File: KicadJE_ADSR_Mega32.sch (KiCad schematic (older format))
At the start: 68 parts, among them J102 OUT2, J105 IN1, J106 IN2, J107 CV2, J108 CV1

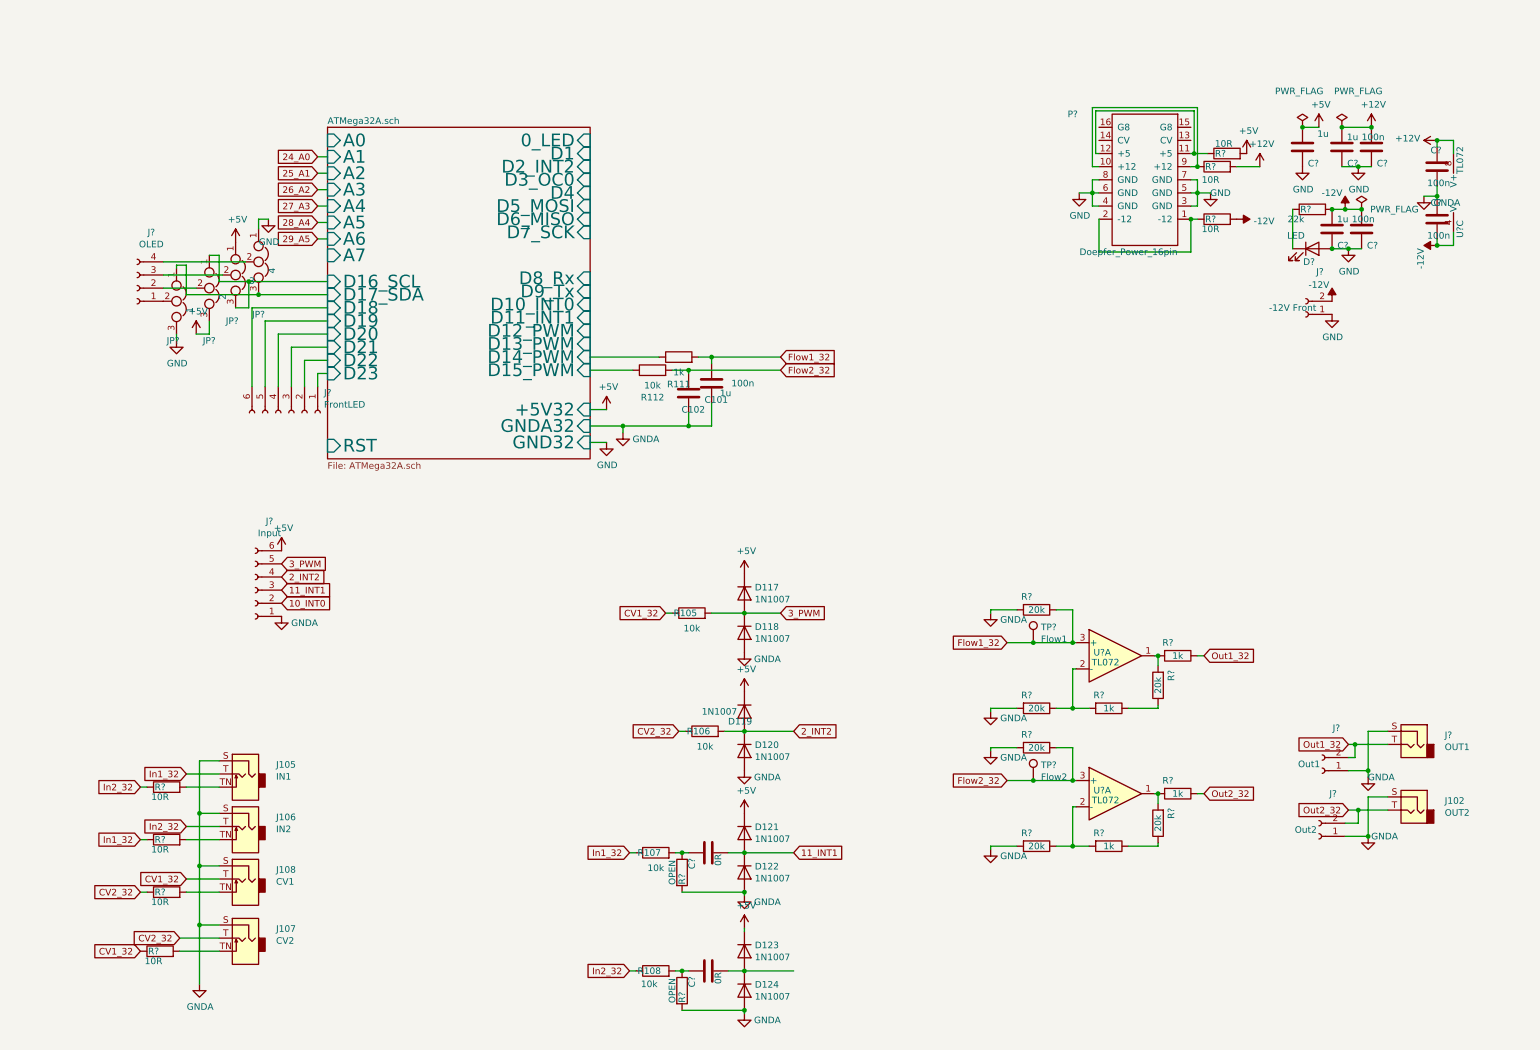
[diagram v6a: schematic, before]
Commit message: Importing Encoder from Midi2CV
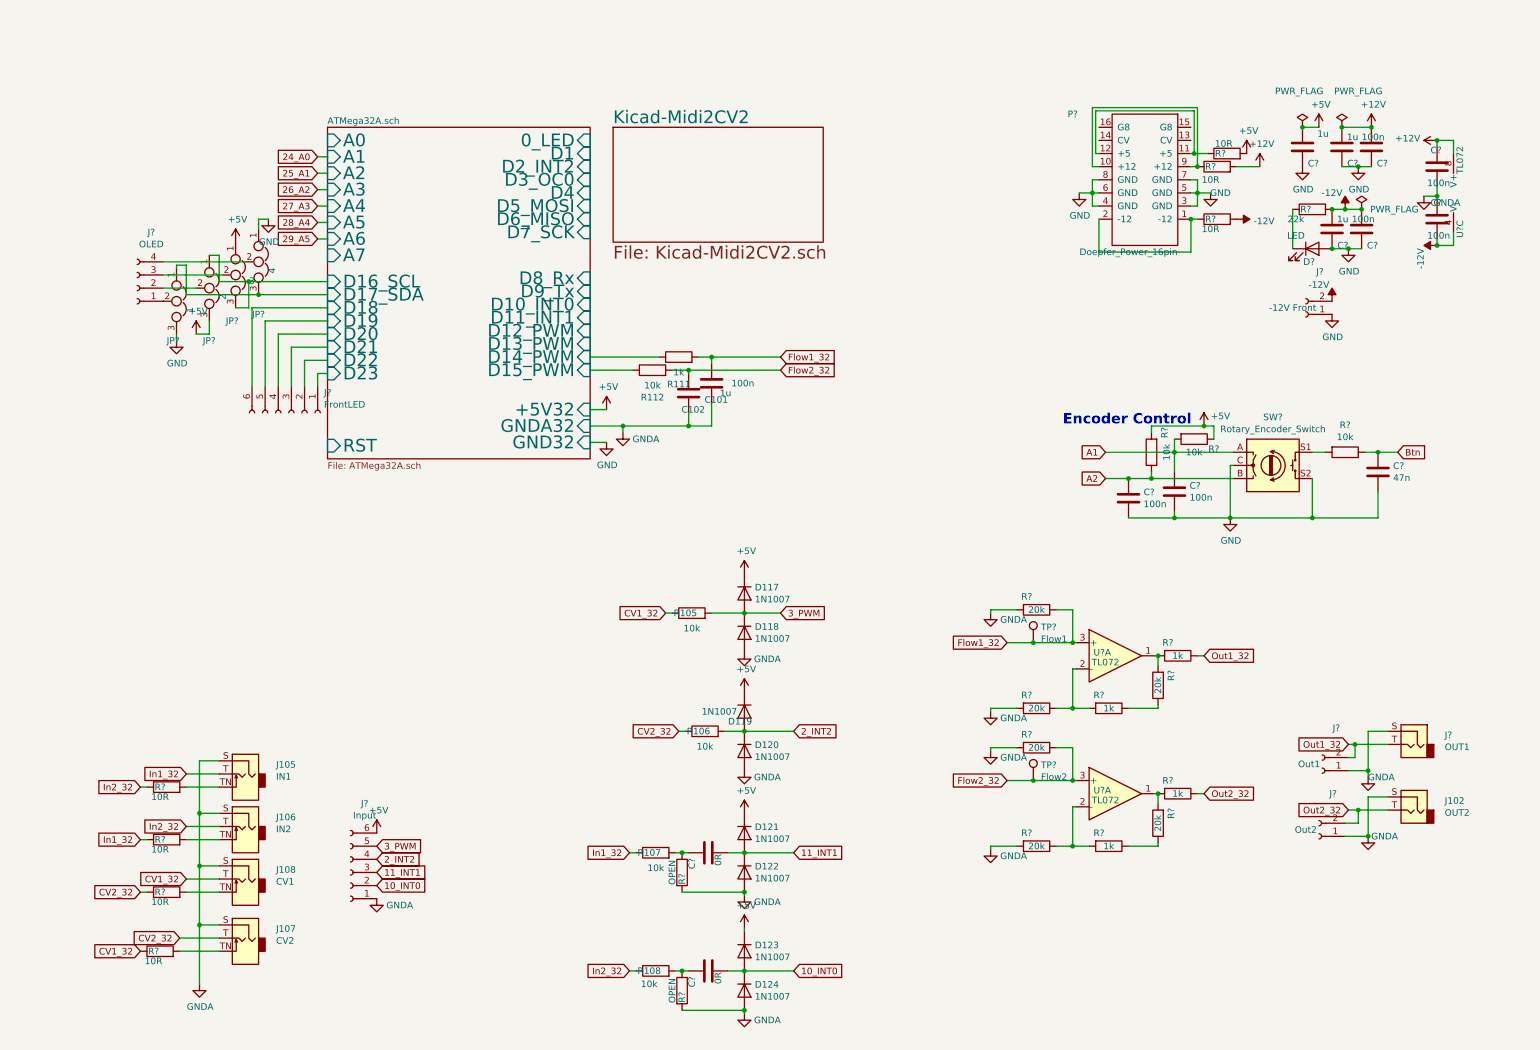
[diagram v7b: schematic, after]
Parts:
- added C? (x2): 100n, Capacitor_SMD:C_0805_2012Metric_Pad1.15x1.40mm_HandSolder, symbol Device:C
- added C?: 47n, Capacitor_SMD:C_0805_2012Metric_Pad1.15x1.40mm_HandSolder, symbol Device:C
- added R? (x3): 10k, Resistor_SMD:R_0805_2012Metric_Pad1.15x1.40mm_HandSolder, symbol Device:R
- added SW?: Rotary_Encoder_Switch, Rotary_Encoder:RotaryEncoder_Alps_EC11E-Switch_Vertical_H20mm, symbol Device:Rotary_Encoder_Switch
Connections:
- net +5V: now also R?.1, R?.2
- net 10_INT0: now also C?.2, D123.2 (A), D124.1 (K)
- net GND: now also C?.2, C?.2, C?.2, SW?.C, SW?.S2
- new net: R?.2, SW?.S1
- new net A1: C?.1, R?.2, SW?.A
- new net A2: C?.1, R?.1, SW?.B
- new net Btn: C?.1, R?.1
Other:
- note added: "Encoder Control"
- moved on the sheet: J?
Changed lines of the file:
@@
 $Descr A4 11693 8268
 encoding utf-8
-Sheet 2 3
+Sheet 2 4
 Title "Kicad_JE_ADSR_Mega32"
 Date "2019-05-13"
@@
 	1    0    0    -1
 $EndComp
-Text GLabel 2075 4500 2    50   Input ~ 0
+Text GLabel 2800 6650 2    50   Input ~ 0
 10_INT0
 Text GLabel 5975 6400 2    50   Input ~ 0
@@
 AR Path="/5F49A670/60E5BC60" Ref="U?"  Part="3"
 AR Path="/60E5BC60" Ref="U?"  Part="3"
+AR Path="/608CA457/60E5BC60" Ref="U?"  Part="3"
 F 0 "U?" V 10750 1100 50  0000 C CNN
 F 1 "TL072" V 10750 1625 50  0000 C CNN
@@
 L Connector:Conn_01x06_Female J?
 U 1 1 610AFCC8
-P 1875 4400
-F 0 "J?" H 1767 3875 50  0000 C CNN
-F 1 "Input" H 1767 3966 50  0000 C CNN
-F 2 "Connector_PinSocket_2.54mm:PinSocket_1x06_P2.54mm_Vertical" H 1875 4400 50  0001 C CNN
-F 3 "~" H 1875 4400 50  0001 C CNN
-	1    1875 4400
+P 2600 6550
+F 0 "J?" H 2492 6025 50  0000 C CNN
+F 1 "Input" H 2492 6116 50  0000 C CNN
+F 2 "Connector_PinSocket_2.54mm:PinSocket_1x06_P2.54mm_Vertical" H 2600 6550 50  0001 C CNN
+F 3 "~" H 2600 6550 50  0001 C CNN
+	1    2600 6550
 	-1   0    0    1
 $EndComp
-Text GLabel 2075 4200 2    50   Input ~ 0
+Text GLabel 2800 6350 2    50   Input ~ 0
 3_PWM
-Text GLabel 2075 4300 2    50   Input ~ 0
+Text GLabel 2800 6450 2    50   Input ~ 0
 2_INT2
-Text GLabel 2075 4400 2    50   Input ~ 0
+Text GLabel 2800 6550 2    50   Input ~ 0
 11_INT1
 $Comp
 L power:GNDA #PWR?
 U 1 1 610D759E
-P 2075 4600
+P 2800 6750
 AR Path="/610D759E" Ref="#PWR?"  Part="1"
 AR Path="/5CD3F059/610D759E" Ref="#PWR?"  Part="1"
 AR Path="/608CA457/610D759E" Ref="#PWR?"  Part="1"
-F 0 "#PWR?" H 2075 4350 50  0001 C CNN
-F 1 "GNDA" H 2250 4550 50  0000 C CNN
-F 2 "" H 2075 4600 50  0001 C CNN
-F 3 "" H 2075 4600 50  0001 C CNN
-	1    2075 4600
+F 0 "#PWR?" H 2800 6500 50  0001 C CNN
+F 1 "GNDA" H 2975 6700 50  0000 C CNN
+F 2 "" H 2800 6750 50  0001 C CNN
+F 3 "" H 2800 6750 50  0001 C CNN
+	1    2800 6750
 	1    0    0    -1
 $EndComp
@@
 L power:+5V #PWR?
 U 1 1 610D7AE4
-P 2075 4100
-F 0 "#PWR?" H 2075 3950 50  0001 C CNN
-F 1 "+5V" H 2090 4273 50  0000 C CNN
-F 2 "" H 2075 4100 50  0001 C CNN
-F 3 "" H 2075 4100 50  0001 C CNN
-	1    2075 4100
+P 2800 6250
+F 0 "#PWR?" H 2800 6100 50  0001 C CNN
+F 1 "+5V" H 2815 6423 50  0000 C CNN
+F 2 "" H 2800 6250 50  0001 C CNN
+F 3 "" H 2800 6250 50  0001 C CNN
+	1    2800 6250
 	1    0    0    -1
 $EndComp
@@
 	1    0    0    -1
 $EndComp
+$Sheet
+S 4600 875  1600 875
+U 6120CBE2
+F0 "Kicad-Midi2CV2" 97
+F1 "Kicad-Midi2CV2.sch" 97
+$EndSheet
+$Comp
+L Device:C C?
+U 1 1 6125DC4B
+P 8525 3700
+F 0 "C?" H 8640 3746 50  0000 L CNN
+F 1 "100n" H 8640 3655 50  0000 L CNN
+F 2 "Capacitor_SMD:C_0805_2012Metric_Pad1.15x1.40mm_HandSolder" H 8563 3550 50  0001 C CNN
+F 3 "~" H 8525 3700 50  0001 C CNN
+	1    8525 3700
+	1    0    0    -1
+$EndComp
+$Comp
+L Device:C C?
+U 1 1 6125DC51
+P 8875 3650
+F 0 "C?" H 8990 3696 50  0000 L CNN
+F 1 "100n" H 8990 3605 50  0000 L CNN
+F 2 "Capacitor_SMD:C_0805_2012Metric_Pad1.15x1.40mm_HandSolder" H 8913 3500 50  0001 C CNN
+F 3 "~" H 8875 3650 50  0001 C CNN
+	1    8875 3650
+	1    0    0    -1
+$EndComp
+Text GLabel 10575 3350 2    50   Input ~ 0
+Btn
+$Comp
+L power:GND #PWR?
+U 1 1 6125DC58
+P 9300 3850
+F 0 "#PWR?" H 9300 3600 50  0001 C CNN
+F 1 "GND" H 9305 3677 50  0000 C CNN
+F 2 "" H 9300 3850 50  0001 C CNN
+F 3 "" H 9300 3850 50  0001 C CNN
+	1    9300 3850
+	1    0    0    -1
+$EndComp
+$Comp
+L Device:R R?
+U 1 1 6125DC5E
+P 10175 3350
+F 0 "R?" V 9968 3350 50  0000 C CNN
+F 1 "10k" V 10059 3350 50  0000 C CNN
+F 2 "Resistor_SMD:R_0805_2012Metric_Pad1.15x1.40mm_HandSolder" V 10105 3350 50  0001 C CNN
+F 3 "~" H 10175 3350 50  0001 C CNN
+	1    10175 3350
+	0    1    1    0
+$EndComp
+$Comp
+L Device:C C?
+U 1 1 6125DC64
+P 10425 3500
+F 0 "C?" H 10540 3546 50  0000 L CNN
+F 1 "47n" H 10540 3455 50  0000 L CNN
+F 2 "Capacitor_SMD:C_0805_2012Metric_Pad1.15x1.40mm_HandSolder" H 10463 3350 50  0001 C CNN
+F 3 "~" H 10425 3500 50  0001 C CNN
+	1    10425 3500
+	1    0    0    -1
+$EndComp
+Text GLabel 8350 3350 0    50   Input ~ 0
+A1
+Text Notes 8025 3150 0    79   ~ 16
+Encoder Control
+Text GLabel 8350 3550 0    50   Input ~ 0
+A2
+Wire Wire Line
+	9925 3550 9925 3850
+$Comp
+L power:+5V #PWR?
+U 1 1 6125DC71
+P 9100 3150
+F 0 "#PWR?" H 9100 3000 50  0001 C CNN
+F 1 "+5V" H 9225 3225 50  0000 C CNN
+F 2 "" H 9100 3150 50  0001 C CNN
+F 3 "" H 9100 3150 50  0001 C CNN
+	1    9100 3150
+	1    0    0    -1
+$EndComp
+Wire Wire Line
+	9925 3350 10025 3350
+Wire Wire Line
+	10325 3350 10425 3350
+Wire Wire Line
+	10575 3350 10425 3350
+Connection ~ 10425 3350
+Wire Wire Line
+	10425 3650 10425 3850
+Wire Wire Line
+	10425 3850 9925 3850
+Connection ~ 9925 3850
+Wire Wire Line
+	8875 3800 8875 3850
+Connection ~ 8875 3850
+Wire Wire Line
+	8875 3500 8875 3350
+Connection ~ 8875 3350
+Wire Wire Line
+	8875 3350 9325 3350
+$Comp
+L Device:Rotary_Encoder_Switch SW?
+U 1 1 6125DC86
+P 9625 3450
+AR Path="/608CA457/6120CBE2/6125DC86" Ref="SW?"  Part="1"
+AR Path="/608CA457/6125DC86" Ref="SW?"  Part="1"
+F 0 "SW?" H 9625 3817 50  0000 C CNN
+F 1 "Rotary_Encoder_Switch" H 9625 3726 50  0000 C CNN
+F 2 "Rotary_Encoder:RotaryEncoder_Alps_EC11E-Switch_Vertical_H20mm" H 9475 3610 50  0001 C CNN
+F 3 "~" H 9625 3710 50  0001 C CNN
+	1    9625 3450
+	1    0    0    -1
+$EndComp
+Wire Wire Line
+	8525 3850 8875 3850
+Wire Wire Line
+	8875 3850 9300 3850
+Wire Wire Line
+	8350 3550 8525 3550
+Connection ~ 8525 3550
+Wire Wire Line
+	8525 3550 8700 3550
+Wire Wire Line
+	8350 3350 8875 3350
+Wire Wire Line
+	9300 3450 9300 3850
+Wire Wire Line
+	9300 3450 9325 3450
+Connection ~ 9300 3850
+Wire Wire Line
+	9300 3850 9925 3850
+$Comp
+L Device:R R?
+U 1 1 6125DC97
+P 8700 3350
+F 0 "R?" V 8600 3200 50  0000 C CNN
+F 1 "10k" V 8584 3350 50  0000 C CNN
+F 2 "Resistor_SMD:R_0805_2012Metric_Pad1.15x1.40mm_HandSolder" V 8630 3350 50  0001 C CNN
+F 3 "~" H 8700 3350 50  0001 C CNN
+	1    8700 3350
+	-1   0    0    1
+$EndComp
+$Comp
+L Device:R R?
+U 1 1 6125DC9D
+P 9025 3250
+F 0 "R?" V 9100 3400 50  0000 C CNN
+F 1 "10k" V 9125 3250 50  0000 C CNN
+F 2 "Resistor_SMD:R_0805_2012Metric_Pad1.15x1.40mm_HandSolder" V 8955 3250 50  0001 C CNN
+F 3 "~" H 9025 3250 50  0001 C CNN
+	1    9025 3250
+	0    1    1    0
+$EndComp
+Wire Wire Line
+	8700 3550 8700 3500
+Connection ~ 8700 3550
+Wire Wire Line
+	8700 3550 9325 3550
+Wire Wire Line
+	8875 3350 8875 3250
+Wire Wire Line
+	8700 3200 8700 3150
+Wire Wire Line
+	8700 3150 9100 3150
+Wire Wire Line
+	9175 3250 9175 3150
+Wire Wire Line
+	9175 3150 9100 3150
+Connection ~ 9100 3150
+Text GLabel 5975 7300 2    50   Input ~ 0
+10_INT0
 $EndSCHEMATC

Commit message: In/CV+Encoder matched to analog input
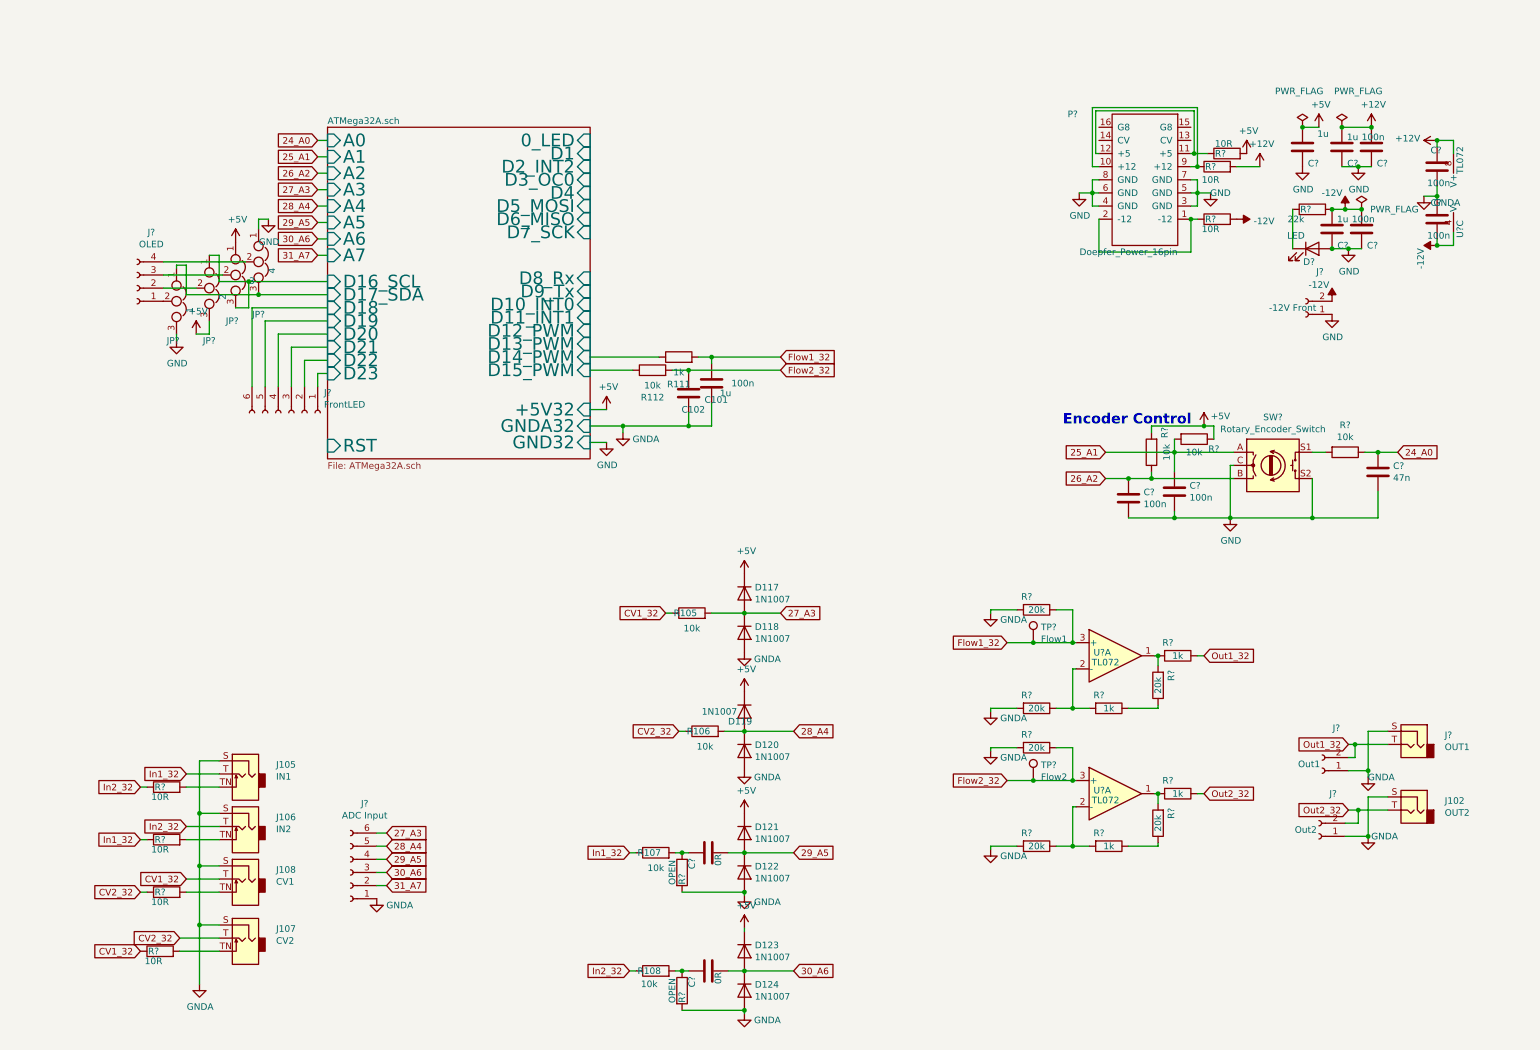
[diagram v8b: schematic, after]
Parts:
- J?: value Input -> ADC Input
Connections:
- net A1 is gone; now on net 25_A1: C?.1, R?.2, SW?.A
- net A2 is gone; now on net 26_A2: C?.1, R?.1, SW?.B
- net Btn is gone; now on net 24_A0: C?.1, R?.1
- net +5V: no longer J?.6 (Pin_6)
- net 27_A3: now also D117.2 (A), D118.1 (K), J?.6 (Pin_6), R105.2
- net 28_A4: now also D119.2 (A), D120.1 (K), J?.5 (Pin_5), R106.2
- net 29_A5: now also C?.2, D121.2 (A), D122.1 (K), J?.4 (Pin_4)
- net 10_INT0 renamed 30_A6
- net 30_A6: now also J?.3 (Pin_3); no longer J?.2 (Pin_2)
- removed net 11_INT1: C?.2, D121.2 (A), D122.1 (K), J?.3 (Pin_3)
- removed net 2_INT2: D119.2 (A), D120.1 (K), J?.4 (Pin_4), R106.2
- removed net 3_PWM: D117.2 (A), D118.1 (K), J?.5 (Pin_5), R105.2
- new net 31_A7: J?.2 (Pin_2)
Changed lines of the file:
@@
 $Descr A4 11693 8268
 encoding utf-8
-Sheet 2 4
+Sheet 2 3
 Title "Kicad_JE_ADSR_Mega32"
 Date "2019-05-13"
@@
 F37 "D3_OC0" I R 4425 1275 97
 $EndSheet
-Text GLabel 5975 5475 2    50   Input ~ 0
-2_INT2
 $Comp
 L Connector:AudioJack2 J102
@@
 	1    0    0    -1
 $EndComp
-Text GLabel 2800 6650 2    50   Input ~ 0
-10_INT0
-Text GLabel 5975 6400 2    50   Input ~ 0
-11_INT1
 $Comp
 L Connector:AudioJack2_SwitchT J105
@@
 Wire Wire Line
 	5475 7300 5600 7300
-Text GLabel 5875 4575 2    50   Input ~ 0
-3_PWM
 Wire Wire Line
 	1600 6950 1450 6950
@@
 	1    0    0    -1
 $EndComp
+Text GLabel 2350 975  0    50   Input ~ 0
+24_A0
 Text GLabel 2350 1100 0    50   Input ~ 0
-24_A0
+25_A1
 Text GLabel 2350 1225 0    50   Input ~ 0
-25_A1
+26_A2
 Text GLabel 2350 1350 0    50   Input ~ 0
-26_A2
+27_A3
 Text GLabel 2350 1475 0    50   Input ~ 0
-27_A3
+28_A4
 Text GLabel 2350 1600 0    50   Input ~ 0
-28_A4
-Text GLabel 2350 1725 0    50   Input ~ 0
 29_A5
 $Comp
@@
 	1    0    0    -1
 $EndComp
-Wire Wire Line
-	2350 1725 2425 1725
 Wire Wire Line
 	2425 1600 2350 1600
@@
 P 2600 6550
 F 0 "J?" H 2492 6025 50  0000 C CNN
-F 1 "Input" H 2492 6116 50  0000 C CNN
+F 1 "ADC Input" H 2492 6116 50  0000 C CNN
 F 2 "Connector_PinSocket_2.54mm:PinSocket_1x06_P2.54mm_Vertical" H 2600 6550 50  0001 C CNN
 F 3 "~" H 2600 6550 50  0001 C CNN
@@
 	-1   0    0    1
 $EndComp
-Text GLabel 2800 6350 2    50   Input ~ 0
-3_PWM
-Text GLabel 2800 6450 2    50   Input ~ 0
-2_INT2
-Text GLabel 2800 6550 2    50   Input ~ 0
-11_INT1
 $Comp
 L power:GNDA #PWR?
@@
 F 3 "" H 2800 6750 50  0001 C CNN
 	1    2800 6750
-	1    0    0    -1
-$EndComp
-$Comp
-L power:+5V #PWR?
-U 1 1 610D7AE4
-P 2800 6250
-F 0 "#PWR?" H 2800 6100 50  0001 C CNN
-F 1 "+5V" H 2815 6423 50  0000 C CNN
-F 2 "" H 2800 6250 50  0001 C CNN
-F 3 "" H 2800 6250 50  0001 C CNN
-	1    2800 6250
 	1    0    0    -1
 $EndComp
@@
 	1    0    0    -1
 $EndComp
-$Sheet
-S 4600 875  1600 875
-U 6120CBE2
-F0 "Kicad-Midi2CV2" 97
-F1 "Kicad-Midi2CV2.sch" 97
-$EndSheet
 $Comp
 L Device:C C?
@@
 	1    0    0    -1
 $EndComp
-Text GLabel 10575 3350 2    50   Input ~ 0
-Btn
 $Comp
 L power:GND #PWR?
@@
 	1    0    0    -1
 $EndComp
-Text GLabel 8350 3350 0    50   Input ~ 0
-A1
 Text Notes 8025 3150 0    79   ~ 16
 Encoder Control
-Text GLabel 8350 3550 0    50   Input ~ 0
-A2
 Wire Wire Line
 	9925 3550 9925 3850
@@
 	9175 3150 9100 3150
 Connection ~ 9100 3150
+Text GLabel 8350 3350 0    50   Input ~ 0
+25_A1
+Wire Wire Line
+	2350 975  2425 975
+Text GLabel 2350 1725 0    50   Input ~ 0
+30_A6
+Text GLabel 2350 1850 0    50   Input ~ 0
+31_A7
+Wire Wire Line
+	2425 1850 2350 1850
+Wire Wire Line
+	2350 1725 2425 1725
+Text GLabel 8350 3550 0    50   Input ~ 0
+26_A2
+Text GLabel 10575 3350 2    50   Input ~ 0
+24_A0
+Text GLabel 5875 4575 2    50   Input ~ 0
+27_A3
+Text GLabel 5975 5475 2    50   Input ~ 0
+28_A4
+Text GLabel 5975 6400 2    50   Input ~ 0
+29_A5
 Text GLabel 5975 7300 2    50   Input ~ 0
-10_INT0
+30_A6
+Text GLabel 2875 6250 2    50   Input ~ 0
+27_A3
+Text GLabel 2875 6350 2    50   Input ~ 0
+28_A4
+Text GLabel 2875 6450 2    50   Input ~ 0
+29_A5
+Wire Wire Line
+	2800 6450 2875 6450
+Wire Wire Line
+	2875 6350 2800 6350
+Wire Wire Line
+	2800 6250 2875 6250
+Text GLabel 2875 6550 2    50   Input ~ 0
+30_A6
+Text GLabel 2875 6650 2    50   Input ~ 0
+31_A7
+Wire Wire Line
+	2800 6650 2875 6650
+Wire Wire Line
+	2875 6550 2800 6550
 $EndSCHEMATC
